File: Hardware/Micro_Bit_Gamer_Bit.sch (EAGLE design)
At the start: 37 parts, among them J1 Pokehome, J2 Pokehome, J3 Pokehome, J4 Pokehome, J5 Pokehome, J6 Pokehome, J7 Pokehome, J8 Pokehome, U2 micro:bit

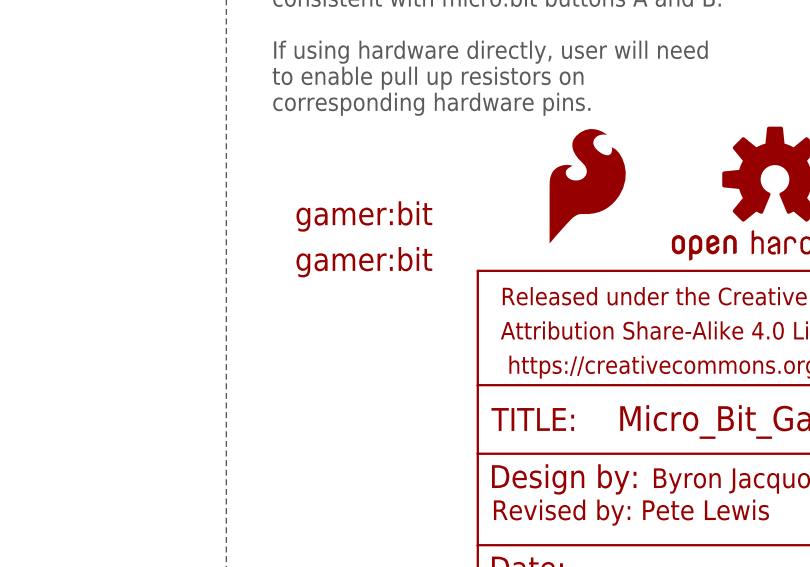
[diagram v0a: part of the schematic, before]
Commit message: Update silk to control bit
On both front and back.
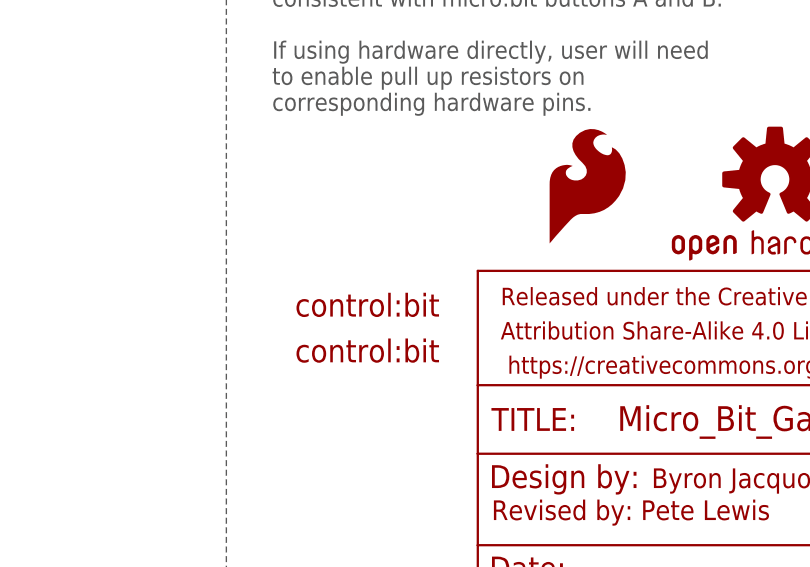
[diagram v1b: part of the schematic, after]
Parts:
- removed U$2, U$3: LOGO-GAMERBIT, Micro_Bit_Parts:LOGO-GAMERBIT
- added U$4, U$5: LOGO-CONTROLBIT, Micro_Bit_Parts:LOGO-CONTROLBIT
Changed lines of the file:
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@@
 <part name="FD3" library="SparkFun-Aesthetics" deviceset="FIDUCIAL" device="UFIDUCIAL"/>
 <part name="FD4" library="SparkFun-Aesthetics" deviceset="FIDUCIAL" device="UFIDUCIAL"/>
-<part name="U$2" library="Micro_Bit_Parts" deviceset="LOGO-GAMERBIT" device=""/>
-<part name="U$3" library="Micro_Bit_Parts" deviceset="LOGO-GAMERBIT" device=""/>
 <part name="U2" library="SparkFun-Connectors" deviceset="MICRO:BIT*?" device="_RA" value="micro:bit"/>
+<part name="U$4" library="Micro_Bit_Parts" deviceset="LOGO-CONTROLBIT" device=""/>
+<part name="U$5" library="Micro_Bit_Parts" deviceset="LOGO-CONTROLBIT" device=""/>
 </parts>
 <sheets>
@@
 <instance part="FD3" gate="G$1" x="243.84" y="27.94" smashed="yes"/>
 <instance part="FD4" gate="G$1" x="243.84" y="25.4" smashed="yes"/>
-<instance part="U$2" gate="G$1" x="127" y="40.64" smashed="yes"/>
-<instance part="U$3" gate="G$1" x="127" y="35.56" smashed="yes"/>
 <instance part="U2" gate="G$1" x="27.94" y="35.56" smashed="yes">
 <attribute name="VALUE" x="10.16" y="6.858" size="1.778" layer="96" align="top-left"/>
 <attribute name="NAME" x="10.16" y="66.04" size="1.778" layer="95" align="top-left"/>
 </instance>
+<instance part="U$4" gate="G$1" x="127" y="30.48" smashed="yes"/>
+<instance part="U$5" gate="G$1" x="127" y="25.4" smashed="yes"/>
 </instances>
 <busses>

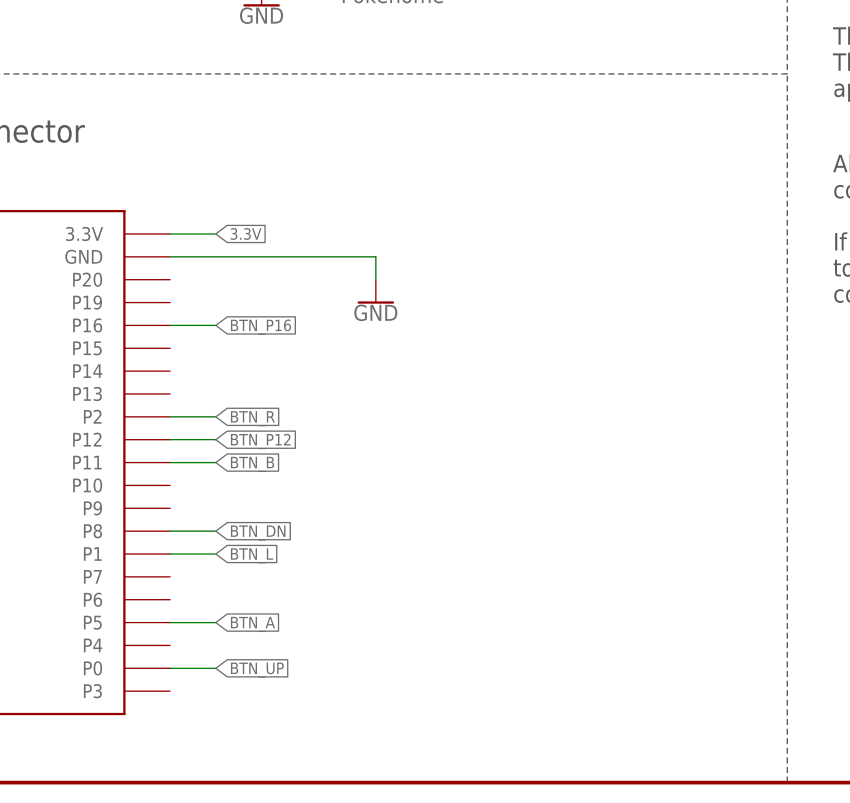
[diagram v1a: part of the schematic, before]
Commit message: Added qwiic connector to back side
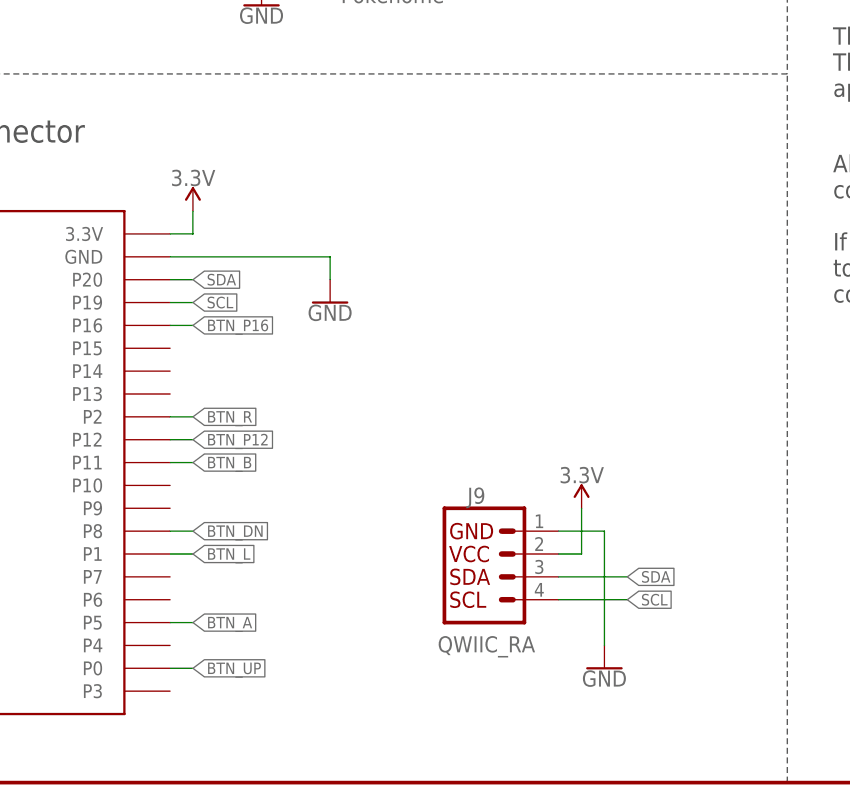
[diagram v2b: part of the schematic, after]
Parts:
- added J9: QWIIC_RA, SparkFun-Connectors:QWIIC_CONNECTORJS-1MM
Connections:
- new net SCL: J9.4, U2.P19
- new net SDA: J9.3, U2.P20
- net 3.3V: now also J9.2
- net GND: now also J9.1
